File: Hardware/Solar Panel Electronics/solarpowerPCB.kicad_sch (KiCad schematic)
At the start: 41 parts, among them J3 Conn_01x02_Male, J4 Conn_01x06_Male, J5 Conn_01x02_Male, Q1 MMDT2222A, U1 SN65HVD230, U2 ESP32-PICO-D4

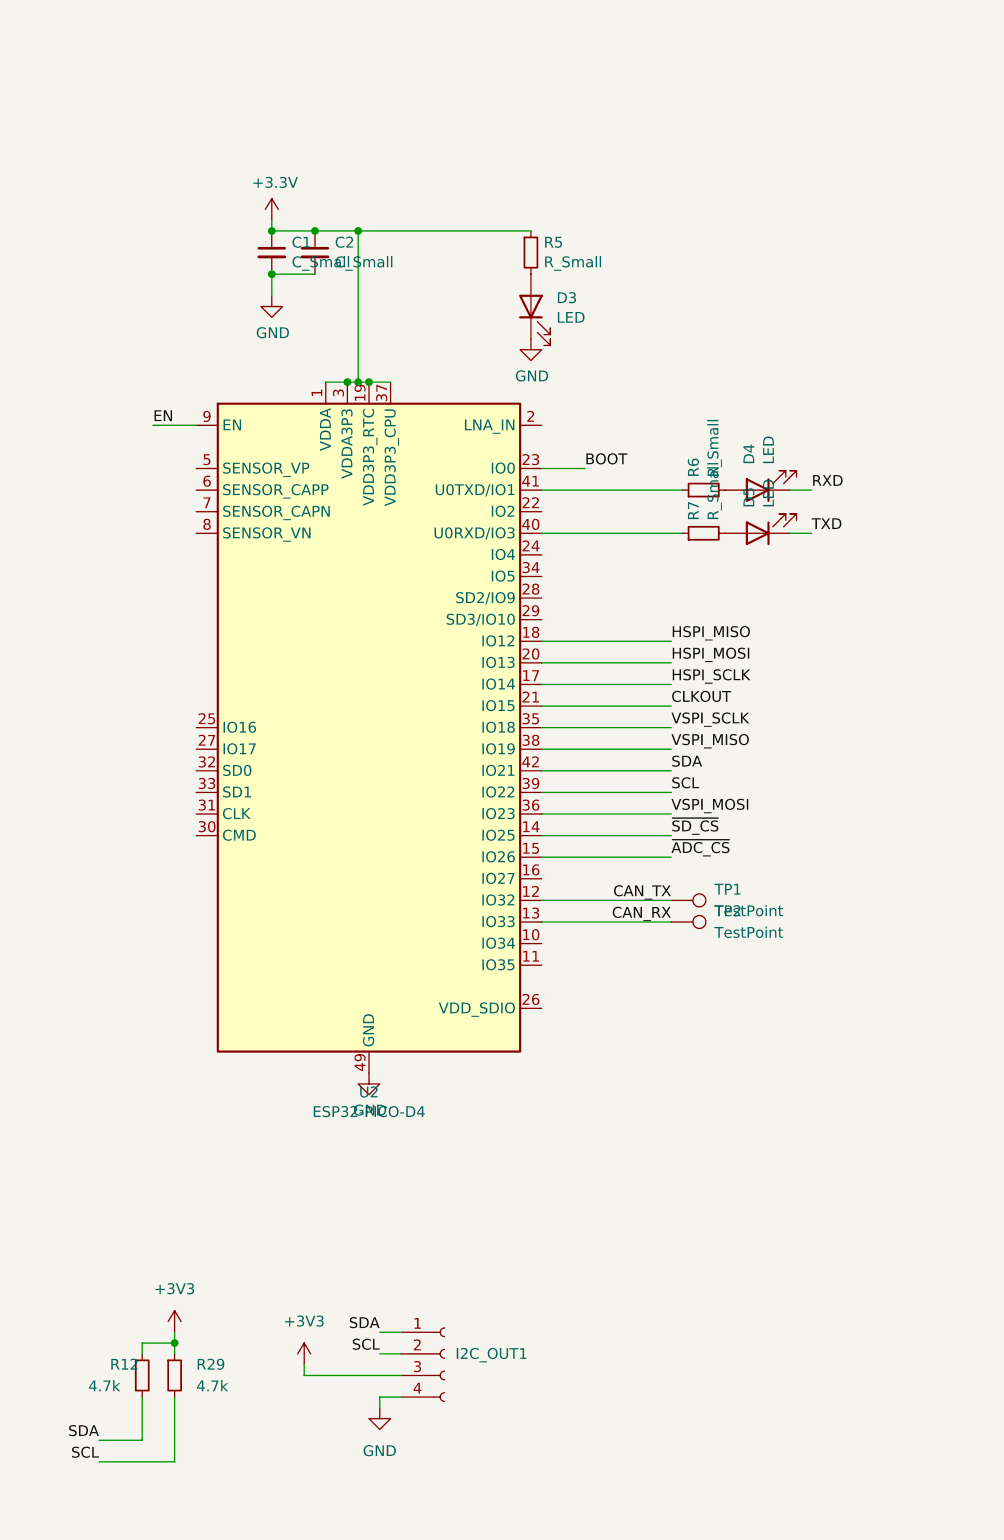
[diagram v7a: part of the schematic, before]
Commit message: Add Antenna
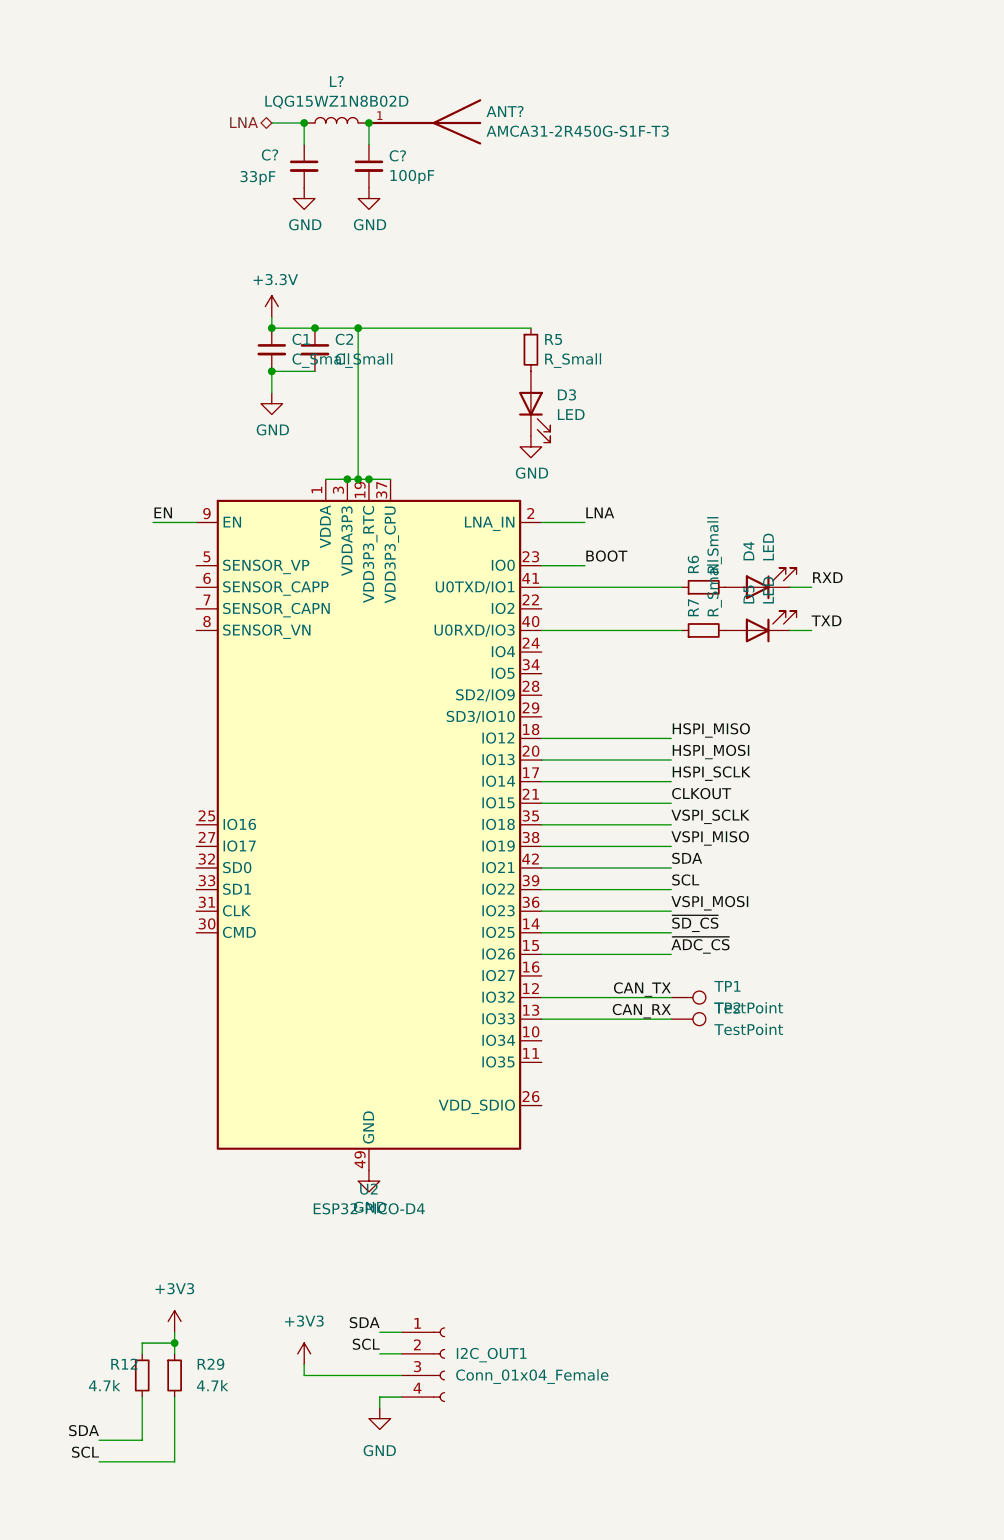
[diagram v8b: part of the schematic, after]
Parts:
- added ANT?: AMCA31-2R450G-S1F-T3, iclr:ANT_AMCA31-2R450G-S1F-T3, symbol iclr:AMCA31-2R450G-S1F-T3
- added C?: 100pF, Capacitor_SMD:C_0603_1608Metric, symbol Device:C_Small
- added C?: 33pF, Capacitor_SMD:C_0603_1608Metric, symbol Device:C_Small
- added L?: LQG15WZ1N8B02D, Inductor_SMD:L_0603_1608Metric_Pad1.05x0.95mm_HandSolder, symbol Device:L
- C1, C2: footprint (none) -> Capacitor_SMD:C_0603_1608Metric
- D3, D4, D5: footprint (none) -> LED_SMD:LED_0603_1608Metric
- I2C_OUT1: value (none) -> Conn_01x04_Female; footprint (none) -> Connector_PinSocket_2.54mm:PinSocket_1x04_P2.54mm_Vertical
- R12, R29, R5, R6, R7: footprint (none) -> Resistor_SMD:R_0603_1608Metric
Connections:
- net GND: now also C?.2, C?.2
- net LNA: now reaches U2.2 (LNA_IN)
- net LNA: now also C?.1, L?.1
- new net: ANT?.1, C?.1, L?.2
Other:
- moved on the sheet: C1, C2, D3, D4, D5, R5, R6, R7, TP1, TP2, U2
